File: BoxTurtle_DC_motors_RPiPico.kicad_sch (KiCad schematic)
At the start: 39 parts, among them J1 Power input, J10 DC motor 1, J11 DC motor 2, J12 DC motor 3, J13 DC motor 4, J14 Screw_Terminal_01x02, J15 CAN, J2 Power input, J3 Power output, J4 Power output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

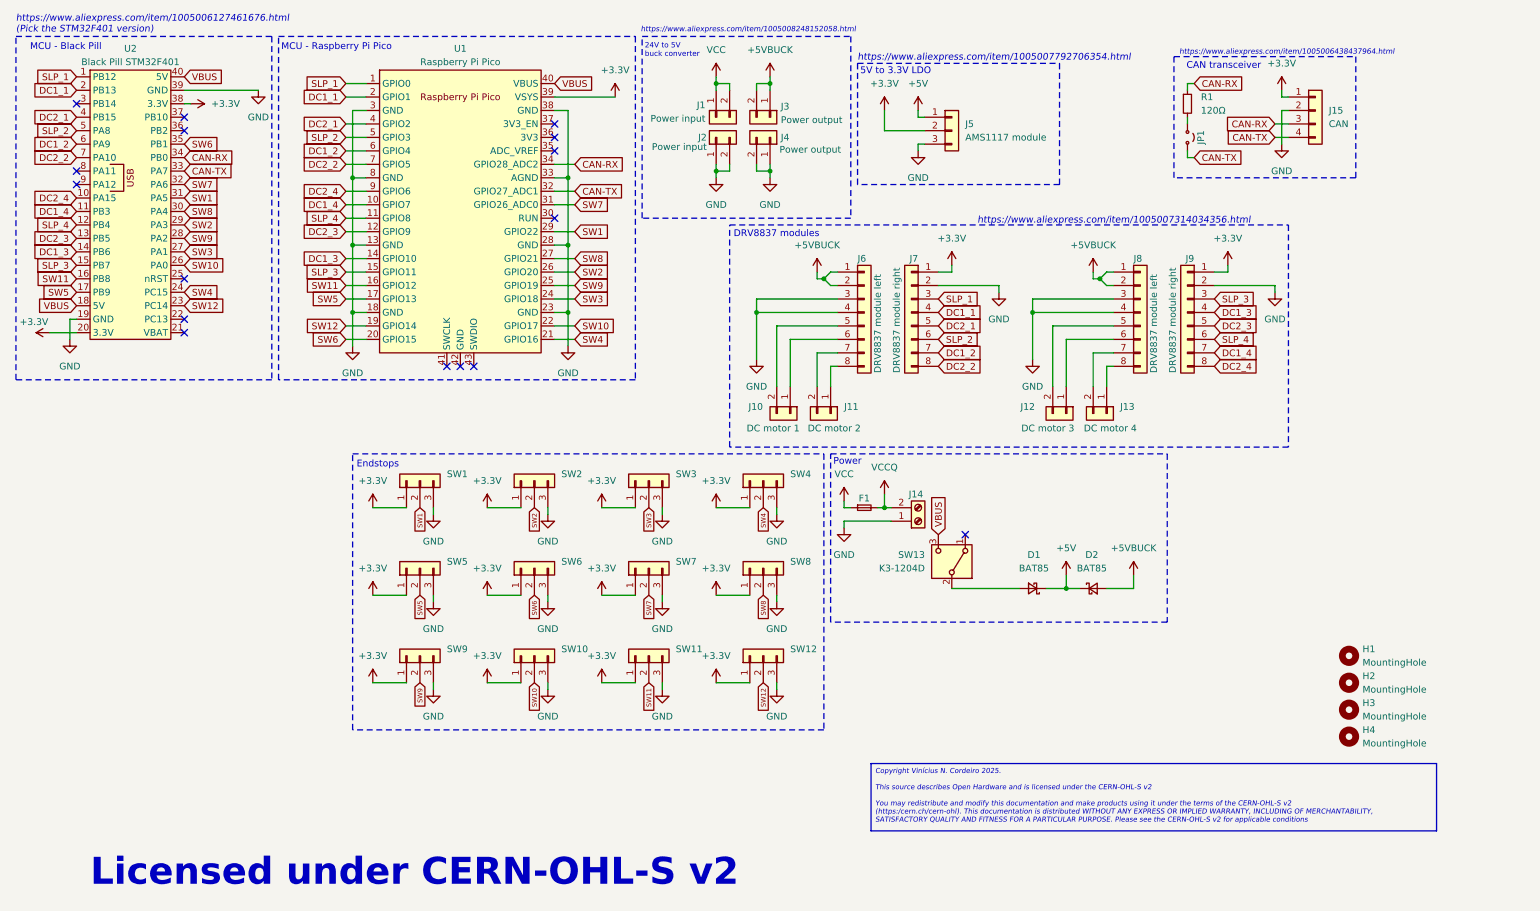
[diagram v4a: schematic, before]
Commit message: Revision 2.6.2
1. adjusted sockets for buck converter; 2. adjusted endstops to follow same pattern as AFC Lite
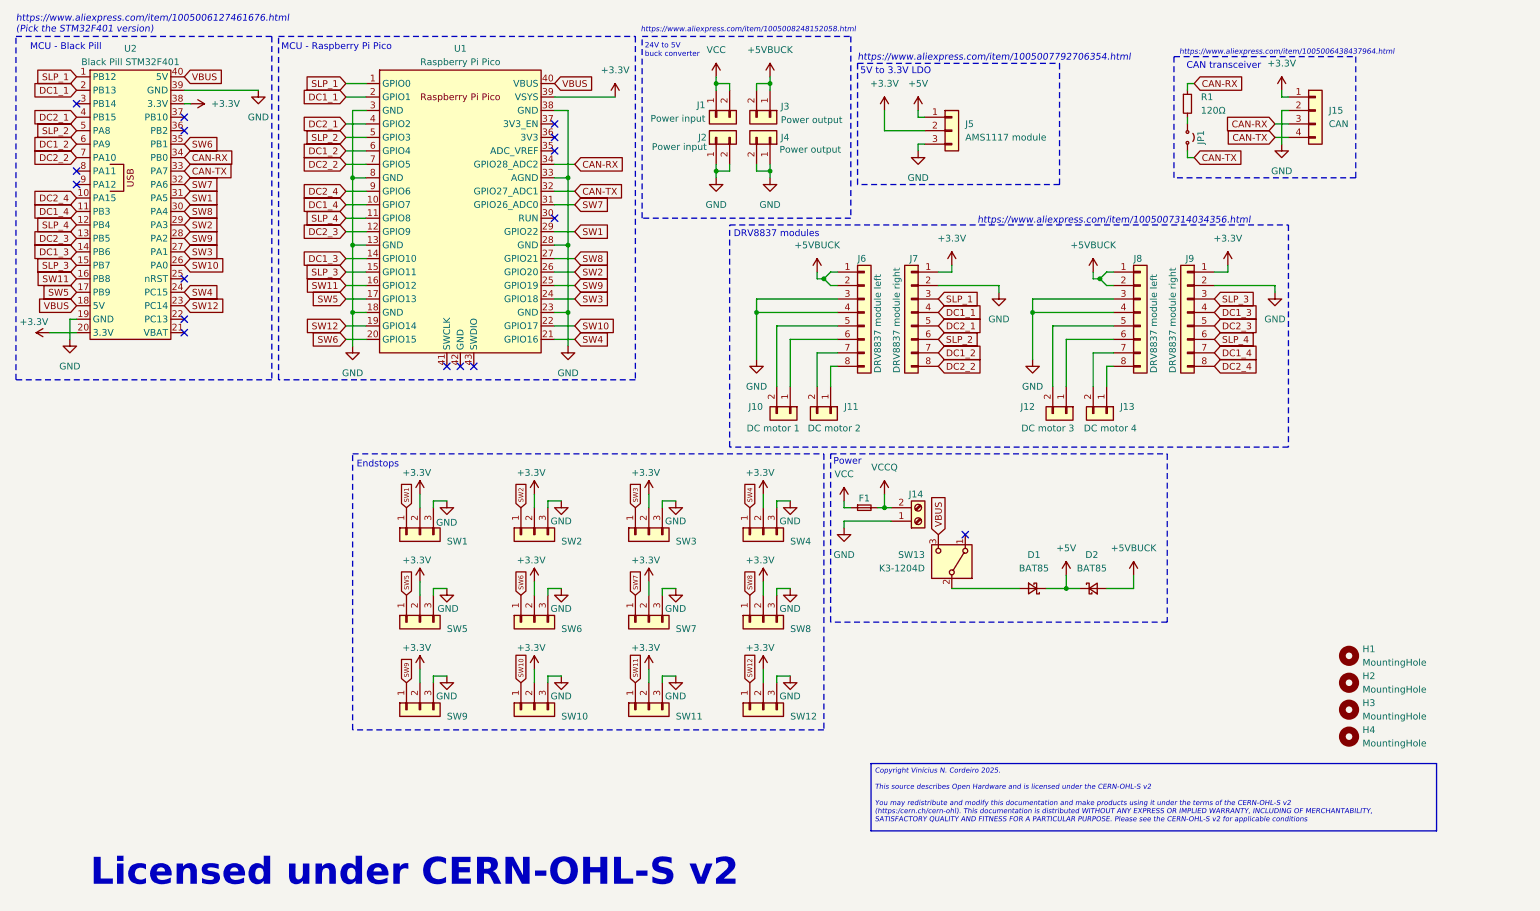
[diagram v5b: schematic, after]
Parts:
- SW13: LCSC C273395 -> C145861
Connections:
- net +3.3V: now also SW1.2 (Pin_2), SW10.2 (Pin_2), SW11.2 (Pin_2), SW12.2 (Pin_2), SW2.2 (Pin_2), SW3.2 (Pin_2), SW4.2 (Pin_2), SW5.2 (Pin_2), SW6.2 (Pin_2), SW7.2 (Pin_2), SW8.2 (Pin_2), SW9.2 (Pin_2); no longer SW1.1 (Pin_1), SW10.1 (Pin_1), SW11.1 (Pin_1), SW12.1 (Pin_1), SW2.1 (Pin_1), SW3.1 (Pin_1), SW4.1 (Pin_1), SW5.1 (Pin_1), SW6.1 (Pin_1), SW7.1 (Pin_1), SW8.1 (Pin_1), SW9.1 (Pin_1)
- net SW1: now also SW1.1 (Pin_1); no longer SW1.2 (Pin_2)
- net SW10: now also SW10.1 (Pin_1); no longer SW10.2 (Pin_2)
- net SW11: now also SW11.1 (Pin_1); no longer SW11.2 (Pin_2)
- net SW12: now also SW12.1 (Pin_1); no longer SW12.2 (Pin_2)
- net SW2: now also SW2.1 (Pin_1); no longer SW2.2 (Pin_2)
- net SW3: now also SW3.1 (Pin_1); no longer SW3.2 (Pin_2)
- net SW4: now also SW4.1 (Pin_1); no longer SW4.2 (Pin_2)
- net SW5: now also SW5.1 (Pin_1); no longer SW5.2 (Pin_2)
- net SW6: now also SW6.1 (Pin_1); no longer SW6.2 (Pin_2)
- net SW7: now also SW7.1 (Pin_1); no longer SW7.2 (Pin_2)
- net SW8: now also SW8.1 (Pin_1); no longer SW8.2 (Pin_2)
- net SW9: now also SW9.1 (Pin_1); no longer SW9.2 (Pin_2)
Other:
- moved on the sheet: SW1, SW10, SW11, SW12, SW2, SW3, SW4, SW5, SW6, SW7, SW8, SW9

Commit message: Revision 2.6.3
Added a solder jumper for powering the microcontroller board while using CANbus; updated silkscreen.
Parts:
- added JP2: Jumper_2_Small_Open, Jumper:SolderJumper-2_P1.3mm_Open_TrianglePad1.0x1.5mm, symbol Jumper:Jumper_2_Small_Open
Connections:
- net +5V: now also JP2.1 (A)
- net VBUS: now also JP2.2 (B)
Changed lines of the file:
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@@
 	(title_block
 		(title "BoxTurtle DC motors standalone board")
-		(date "2025-02-22")
-		(rev "2.4")
+		(date "2026-05-02")
+		(rev "2.6.3")
 	)
 	(rectangle
@@
 		)
 	)
-	(text_box "Copyright Vinícius N. Cordeiro 2025.\n\nThis source describes Open Hardware and is licensed under the CERN-OHL-S v2\n\nYou may redistribute and modify this documentation and make products using it under the terms of the CERN-OHL-S v2 (https:/cern.ch/cern-ohl). This documentation is distributed WITHOUT ANY EXPRESS OR IMPLIED WARRANTY, INCLUDING OF MERCHANTABILITY, SATISFACTORY QUALITY AND FITNESS FOR A PARTICULAR PURPOSE. Please see the CERN-OHL-S v2 for applicable conditions"
+	(text_box "Copyright Vinícius N. Cordeiro 2026.\n\nThis source describes Open Hardware and is licensed under the CERN-OHL-S v2\n\nYou may redistribute and modify this documentation and make products using it under the terms of the CERN-OHL-S v2 (https:/cern.ch/cern-ohl). This documentation is distributed WITHOUT ANY EXPRESS OR IMPLIED WARRANTY, INCLUDING OF MERCHANTABILITY, SATISFACTORY QUALITY AND FITNESS FOR A PARTICULAR PURPOSE. Please see the CERN-OHL-S v2 for applicable conditions"
 		(exclude_from_sim no)
 		(at 177.8 167.64 0)
@@
 		(stroke
 			(width 0)
-			(type default)
+			(type solid)
 		)
 		(fill
@@
 	(wire
 		(pts
+			(xy 209.55 116.84) (xy 209.55 115.57)
+		)
+		(stroke
+			(width 0)
+			(type default)
+		)
+	)
+	(wire
+		(pts
 			(xy 223.52 92.71) (xy 222.25 92.71)
 		)
@@
 	(wire
 		(pts
+			(xy 215.9 116.84) (xy 217.17 116.84)
+		)
+		(stroke
+			(width 0)
+			(type default)
+		)
+	)
+	(wire
+		(pts
 			(xy 120.65 57.15) (xy 120.65 44.45)
 		)
@@
 	(wire
 		(pts
+			(xy 210.82 116.84) (xy 209.55 116.84)
+		)
+		(stroke
+			(width 0)
+			(type default)
+		)
+	)
+	(wire
+		(pts
 			(xy 138.43 152.4) (xy 138.43 151.13)
 		)
@@
 		)
 	)
+	(global_label "VBUS"
+		(shape input)
+		(at 217.17 116.84 0)
+		(fields_autoplaced yes)
+		(effects
+			(font
+				(size 1.27 1.27)
+			)
+			(justify left)
+		)
+		(property "Intersheetrefs" "${INTERSHEET_REFS}"
+			(at 225.0538 116.84 0)
+			(hide yes)
+			(show_name no)
+			(do_not_autoplace no)
+			(effects
+				(font
+					(size 1.27 1.27)
+				)
+				(justify left)
+			)
+		)
+	)
 	(global_label "SW11"
 		(shape input)
@@
 	)
 	(symbol
+		(lib_name "Jumper_2_Small_Open_1")
+		(lib_id "Jumper:Jumper_2_Small_Open")
+		(at 213.36 116.84 0)
+		(unit 1)
+		(body_style 1)
+		(exclude_from_sim no)
+		(in_bom yes)
+		(on_board yes)
+		(in_pos_files yes)
+		(dnp no)
+		(property "Reference" "JP2"
+			(at 213.36 114.554 0)
+			(show_name no)
+			(do_not_autoplace no)
+			(effects
+				(font
+					(size 1.27 1.27)
+				)
+			)
+		)
+		(property "Value" "Jumper_2_Small_Open"
+			(at 213.36 113.03 0)
+			(hide yes)
+			(show_name no)
+			(do_not_autoplace no)
+			(effects
+				(font
+					(size 1.27 1.27)
+				)
+			)
+		)
+		(property "Footprint" "Jumper:SolderJumper-2_P1.3mm_Open_TrianglePad1.0x1.5mm"
+			(at 213.36 116.84 0)
+			(hide yes)
+			(show_name no)
+			(do_not_autoplace no)
+			(effects
+				(font
+					(size 1.27 1.27)
+				)
+			)
+		)
+		(property "Datasheet" ""
+			(at 213.36 116.84 0)
+			(hide yes)
+			(show_name no)
+			(do_not_autoplace no)
+			(effects
+				(font
+					(size 1.27 1.27)
+				)
+			)
+		)
+		(property "Description" "Jumper, 2-pole, small symbol, open"
+			(at 213.36 116.84 0)
+			(hide yes)
+			(show_name no)
+			(do_not_autoplace no)
+			(effects
+				(font
+					(size 1.27 1.27)
+				)
+			)
+		)
+		(pin "1"
+		)
+		(pin "2"
+		)
+		(instances
+			(project "BoxTurtle_DC_motors_RPiPico"
+				(path "/1d127e4b-8316-4553-8f34-cd4a5b3a4711"
+					(reference "JP2")
+					(unit 1)
+				)
+			)
+		)
+	)
+	(symbol
 		(lib_id "power:GND")
 		(at 97.79 134.62 0)
@@
 					(unit 1)
 				)
+			)
+		)
+	)
+	(symbol
+		(lib_id "power:+5V")
+		(at 209.55 115.57 0)
+		(unit 1)
+		(body_style 1)
+		(exclude_from_sim no)
+		(in_bom yes)
+		(on_board yes)
+		(in_pos_files yes)
+		(dnp no)
+		(fields_autoplaced yes)
+		(property "Reference" "#PWR056"
+			(at 209.55 119.38 0)
+			(hide yes)
+			(show_name no)
+			(do_not_autoplace no)
+			(effects
+				(font
+					(size 1.27 1.27)
+				)
+			)
+		)
+		(property "Value" "+5V"
+			(at 209.55 110.49 0)
+			(show_name no)
+			(do_not_autoplace no)
+			(effects
+				(font
+					(size 1.27 1.27)
+				)
+			)
+		)
+		(property "Footprint" ""
+			(at 209.55 115.57 0)
+			(hide yes)
+			(show_name no)
+			(do_not_autoplace no)
+			(effects
+				(font
+					(size 1.27 1.27)
+				)
+			)
+		)
+		(property "Datasheet" ""
+			(at 209.55 115.57 0)
+			(hide yes)
+			(show_name no)
+			(do_not_autoplace no)
+			(effects
+				(font
+					(size 1.27 1.27)
+				)
+			)
+		)
+		(property "Description" "Power symbol creates a global label with name \"+5V\""
+			(at 209.55 115.57 0)
+			(hide yes)
+			(show_name no)
+			(do_not_autoplace no)
+			(effects
+				(font
+					(size 1.27 1.27)
+				)
+			)
+		)
+		(pin "1"
+		)
+		(instances
+			(project "BoxTurtle_DC_motors_RPiPico"
+				(path "/1d127e4b-8316-4553-8f34-cd4a5b3a4711"
+					(reference "#PWR056")
+					(unit 1)
+				)

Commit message: Revision 2.6.4
Will update the Gerber files later
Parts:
- removed JP1: Jumper_2_Small_Open, Connector_PinHeader_2.54mm:PinHeader_1x02_P2.54mm_Vertical, symbol Jumper:Jumper_2_Small_Open
- removed R1: 120Ω, Resistor_THT:R_Axial_DIN0207_L6.3mm_D2.5mm_P10.16mm_Horizontal, symbol Device:R_Small
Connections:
- net at J6.5 (Pin_5): now also J10.1 (Pin_1); no longer J10.2 (Pin_2)
- net at J6.6 (Pin_6): now also J10.2 (Pin_2); no longer J10.1 (Pin_1)
- net at J6.7 (Pin_7): now also J11.1 (Pin_1); no longer J11.2 (Pin_2)
- net at J6.8 (Pin_8): now also J11.2 (Pin_2); no longer J11.1 (Pin_1)
- net at J8.5 (Pin_5): now also J12.1 (Pin_1); no longer J12.2 (Pin_2)
- net at J8.6 (Pin_6): now also J12.2 (Pin_2); no longer J12.1 (Pin_1)
- net at J8.7 (Pin_7): now also J13.1 (Pin_1); no longer J13.2 (Pin_2)
- net at J8.8 (Pin_8): now also J13.2 (Pin_2); no longer J13.1 (Pin_1)
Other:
- moved on the sheet: J10, J11, J12, J13
